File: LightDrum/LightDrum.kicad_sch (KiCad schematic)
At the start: 27 parts, among them U1 24LC04, Y1 16MHz

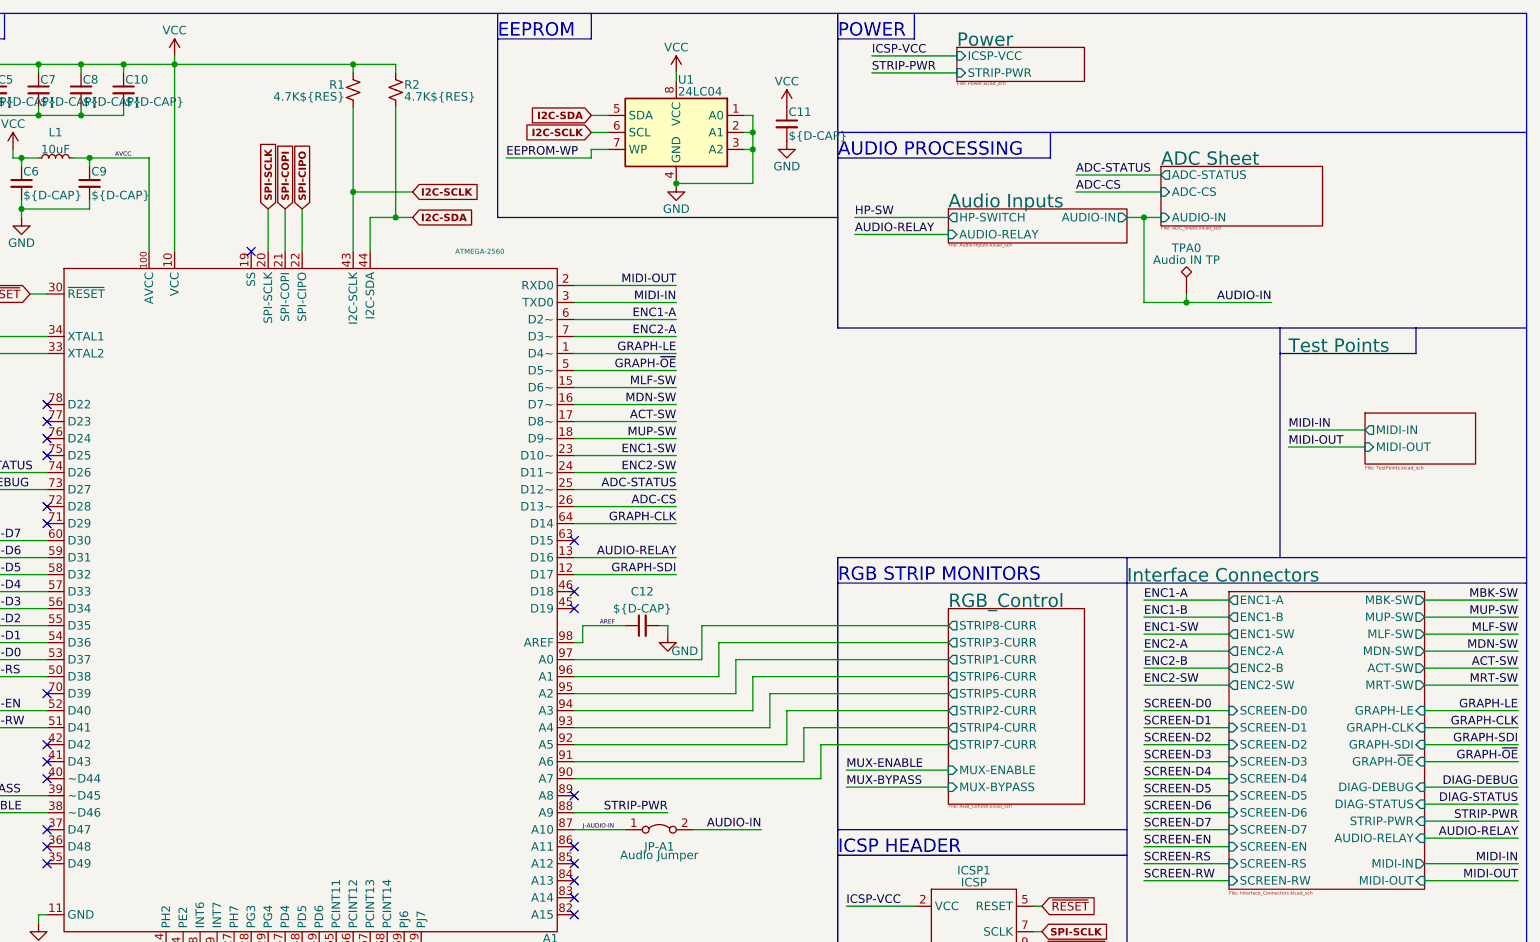
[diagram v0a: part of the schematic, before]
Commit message: Replace interface harnesses with FPC cable
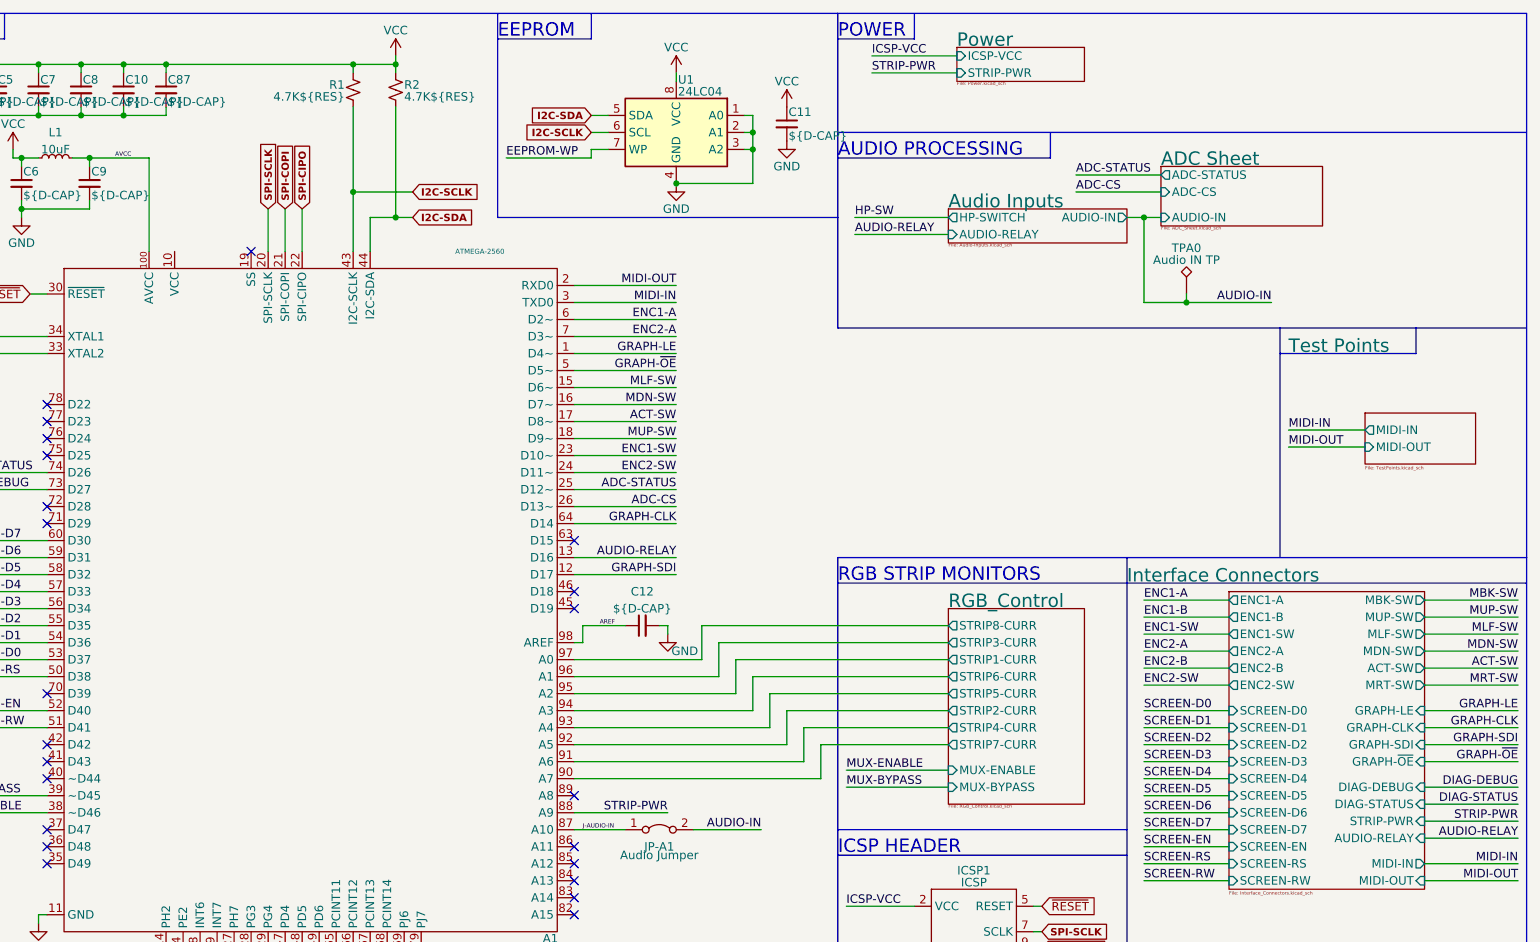
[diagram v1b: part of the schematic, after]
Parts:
- added C87: ${D-CAP}, Capacitor_SMD:C_0603_1608Metric, symbol Device:C_Small
- TPA0: footprint TestPoint:TestPoint_Loop_D2.50mm_Drill1.0mm_LowProfile -> TestPoint:TestPoint_Loop_D2.54mm_Drill1.5mm_Beaded
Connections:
- net GND: now also C87.2
- net VCC: now also C87.1

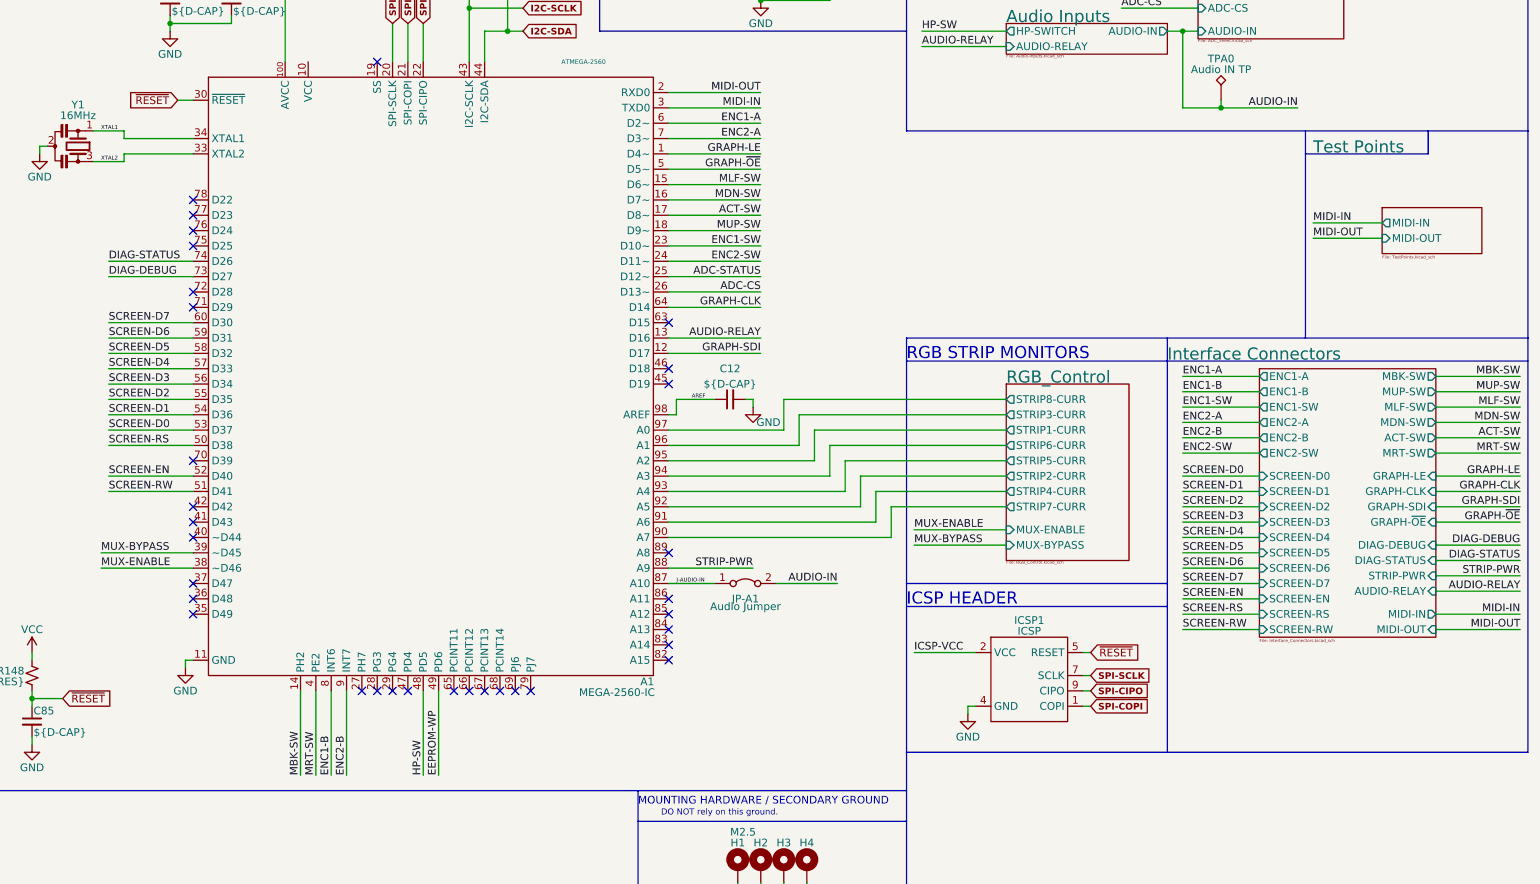
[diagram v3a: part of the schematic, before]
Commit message: Replace screen (WIP)
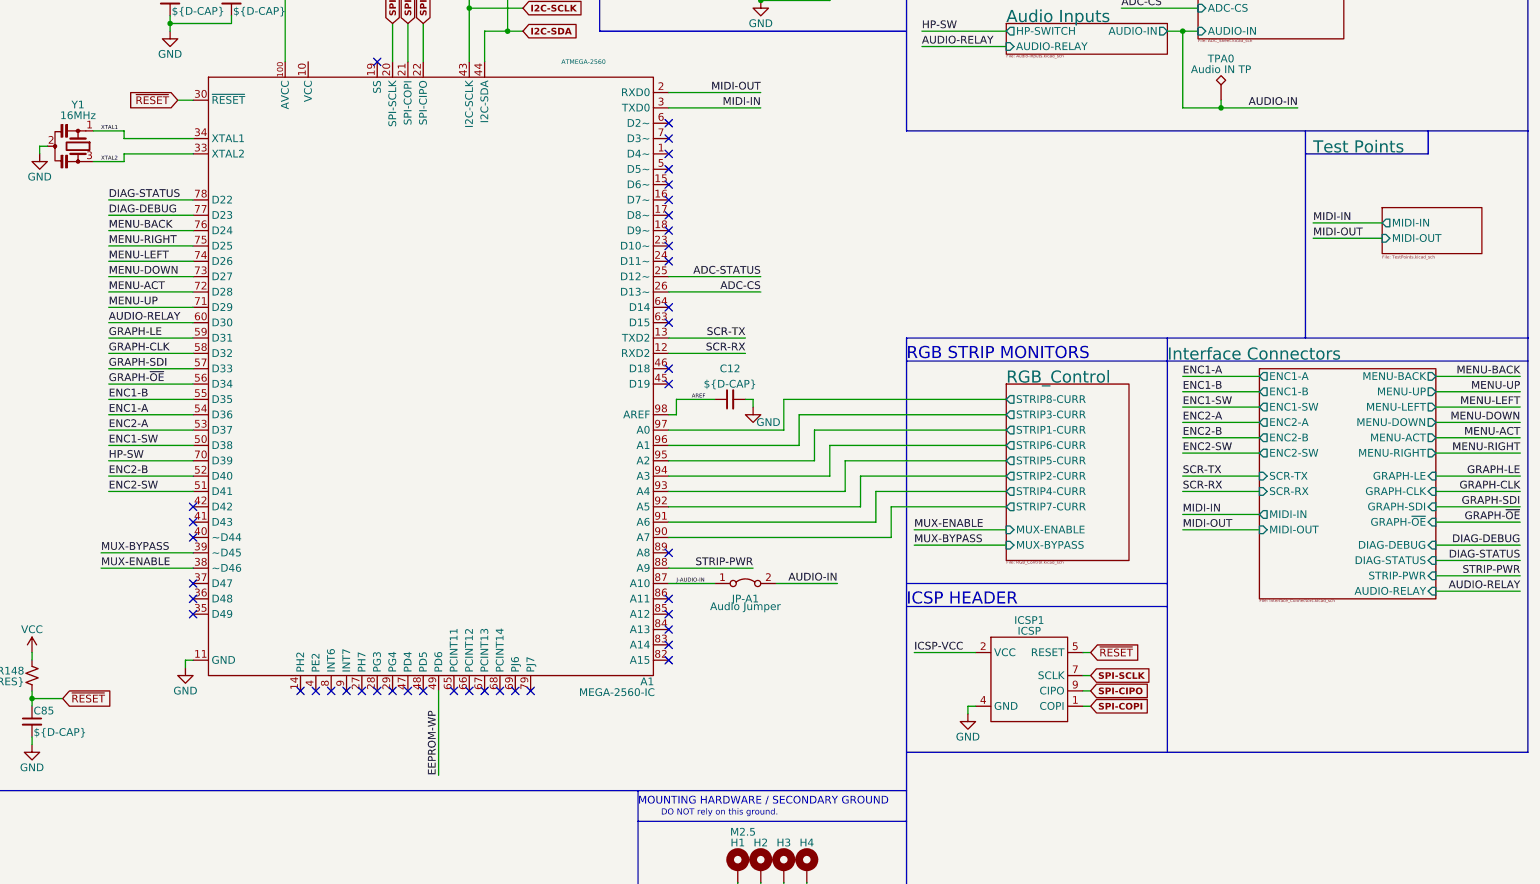
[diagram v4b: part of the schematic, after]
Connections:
- net SCREEN-D0 is gone; now on net ENC2-A: A1.53 (D37)
- net SCREEN-D1 is gone; now on net ENC1-A: A1.54 (D36)
- net SCREEN-D2 is gone; now on net ENC1-B: A1.55 (D35)
- net SCREEN-D3 is gone; now on net GRAPH-~{OE}: A1.56 (D34)
- net SCREEN-D4 is gone; now on net GRAPH-SDI: A1.57 (D33)
- net SCREEN-D5 is gone; now on net GRAPH-CLK: A1.58 (D32)
- net SCREEN-D6 is gone; now on net GRAPH-LE: A1.59 (D31)
- net SCREEN-D7 is gone; now on net AUDIO-RELAY: A1.60 (D30)
- net SCREEN-EN is gone; now on net ENC2-B: A1.52 (D40)
- net SCREEN-RS is gone; now on net ENC1-SW: A1.50 (D38)
- net SCREEN-RW is gone; now on net ENC2-SW: A1.51 (D41)
- net AUDIO-RELAY: no longer A1.13 (D16)
- net DIAG-DEBUG: now also A1.77 (D23); no longer A1.73 (D27)
- net DIAG-STATUS: now also A1.78 (D22); no longer A1.74 (D26)
- net ENC1-A: no longer A1.6 (D2~)
- net ENC1-B: no longer A1.8 (PE6)
- net ENC1-SW: no longer A1.23 (D10~)
- net ENC2-A: no longer A1.7 (D3~)
- net ENC2-B: no longer A1.9 (PE7)
- net ENC2-SW: no longer A1.24 (D11~)
- net GRAPH-CLK: no longer A1.64 (D14)
- net GRAPH-LE: no longer A1.1 (D4~)
- net GRAPH-SDI: no longer A1.12 (D17)
- net GRAPH-~{OE}: no longer A1.5 (D5~)
- net HP-SW: now also A1.70 (D39); no longer A1.48 (PD5)
- net MENU-UP: now reaches A1.71 (D29)
- net MENU-ACT: now reaches A1.72 (D28)
- net MENU-RIGHT: now reaches A1.75 (D25)
- net MENU-BACK: now reaches A1.76 (D24)
- net ACT-SW: no longer names the net of A1.17 (D8~)
- net MBK-SW: no longer names the net of A1.14 (PH2)
- net MDN-SW: no longer names the net of A1.16 (D7~)
- net MLF-SW: no longer names the net of A1.15 (D6~)
- net MRT-SW: no longer names the net of A1.4 (PE2)
- net MUP-SW: no longer names the net of A1.18 (D9~)
- new net MENU-DOWN: A1.73 (D27)
- new net MENU-LEFT: A1.74 (D26)
- new net SCR-RX: A1.12 (D17)
- new net SCR-TX: A1.13 (D16)
- no-connect marks 33 -> 42
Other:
- sheet Interface Connectors ports: added MENU-ACT, MENU-BACK, MENU-DOWN, MENU-LEFT, MENU-RIGHT, MENU-UP, SCR-RX, SCR-TX; removed ACT-SW, MBK-SW, MDN-SW, MLF-SW, MRT-SW, MUP-SW, SCREEN-D0, SCREEN-D1, SCREEN-D2, SCREEN-D3, SCREEN-D4, SCREEN-D5, SCREEN-D6, SCREEN-D7, SCREEN-EN, SCREEN-RS, SCREEN-RW

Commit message: Replaced display and FPC cable
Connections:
- net DIAG-DEBUG: now also A1.78 (D22); no longer A1.77 (D23)
- net DIAG-STATUS: now also A1.77 (D23); no longer A1.78 (D22)
- net MENU-BACK: now also A1.75 (D25); no longer A1.76 (D24)
- net MENU-RIGHT: now also A1.76 (D24); no longer A1.75 (D25)
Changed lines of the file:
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@@
     (effects (font (size 1.27 1.27)) (justify right bottom))
   )
-  (label "MENU-RIGHT" (at 39.37 82.55 0)
+  (label "MENU-RIGHT" (at 39.37 80.01 0)
     (effects (font (size 1.27 1.27)) (justify left bottom))
   )
@@
     (effects (font (size 1.27 1.27)) (justify right bottom))
   )
-  (label "MENU-BACK" (at 39.37 80.01 0)
+  (label "MENU-BACK" (at 39.37 82.55 0)
     (effects (font (size 1.27 1.27)) (justify left bottom))
   )
@@
     (effects (font (size 1.27 1.27)) (justify left bottom))
   )
-  (label "DIAG-STATUS" (at 39.37 74.93 0)
+  (label "DIAG-STATUS" (at 39.37 77.47 0)
     (effects (font (size 1.27 1.27)) (justify left bottom))
   )
@@
     (effects (font (size 1.27 1.27)) (justify right bottom))
   )
-  (label "DIAG-DEBUG" (at 39.37 77.47 0)
+  (label "DIAG-DEBUG" (at 39.37 74.93 0)
     (effects (font (size 1.27 1.27)) (justify left bottom))
   )

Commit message: First pass over schematic (WIP)
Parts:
- removed A1: MEGA-2560-IC, Package_QFP:TQFP-100_14x14mm_P0.5mm, symbol Daxxn_Arduino:MEGA-2560-IC
- removed C12: ${D-CAP}, Capacitor_SMD:C_0603_1608Metric, symbol Device:C_Small
- removed ICSP1: ICSP, Connector:Tag-Connect_TC2050-IDC-FP_2x05_P1.27mm_Vertical, symbol Daxxn_Connectors:ICSP
- removed L1: 10uF, Inductor_SMD:L_1210_3225Metric, symbol Device:L_Small
- removed TPA0: Audio IN TP, TestPoint:TestPoint_Loop_D2.54mm_Drill1.5mm_Beaded, symbol Connector:TestPoint_Alt
- added FB1: 120, Inductor_SMD:L_0603_1608Metric, symbol Device:FerriteBead_Small
- added J10: JTAG, Connector:Tag-Connect_TC2050-IDC-FP_2x05_P1.27mm_Vertical, symbol Connector:Conn_ARM_JTAG_SWD_10
- added J9: VBAT-CONN, symbol Connector:Conn_01x02_Male
- added Q1: RQ5A030AP, Package_TO_SOT_SMD:SOT-23, symbol Daxxn_Transistors:RQ5A030AP
- added R3: 10K, Resistor_SMD:R_0603_1608Metric, symbol Device:R_Small_US
- added SW1: SW_SPDT, Daxxn_Switches:EG1218, symbol Switch:SW_SPDT
- added U2: STM32F103VEH6, Daxxn_Packages:LFBGA-100_P0.8mm, symbol Daxxn_MicroControllers:STM32F103VEH6
- C1, C10, C11, C2, C3, C4, C5, C7, C8, C85, C87: value ${D-CAP} -> 100nF
- C6: value ${D-CAP} -> 10nF; footprint Capacitor_SMD:C_0805_2012Metric -> Capacitor_SMD:C_0603_1608Metric
- C9: value ${D-CAP} -> 100nF; footprint Capacitor_SMD:C_0805_2012Metric -> Capacitor_SMD:C_0603_1608Metric
- R1, R2: value 4.7K${RES} -> 2.2K; footprint Resistor_SMD:R_0805_2012Metric -> Resistor_SMD:R_0603_1608Metric
- R148: value ${P-RES} -> 10K; footprint Resistor_SMD:R_0805_2012Metric -> Resistor_SMD:R_0603_1608Metric
- Y1: value 16MHz -> 8MHz
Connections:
- net ADC-CS: now also U2.K7 (PB12)
- net AUDIO-RELAY: now also U2.B5 (PD5), U2.D7 (PD0)
- net DIAG-DEBUG: now also U2.B6 (PD2)
- net DIAG-STATUS: now also U2.C6 (PD3)
- net EEPROM-WP: now also U2.A3 (PB9)
- net ENC1-A: now also U2.H4 (PE7)
- net ENC1-B: now also U2.E2 (PE6)
- net ENC1-SW: now also U2.K4 (PE9)
- net ENC2-A: now also U2.J4 (PE8)
- net ENC2-B: now also U2.H5 (PE11)
- net ENC2-SW: now also U2.J5 (PE12)
- net GND: now also J10.3 (GND), J10.5 (GND), J10.9 (GNDDetect), Q1.1 (G), SW1.3 (C), U2.C1 (VSS_5), U2.E3 (VSS_4), U2.E4 (VSS_3), U2.E5 (VSS_2), U2.E6 (VSS_1), U2.G0 (VSSA), U2.H0 (VREF-)
- net GRAPH-CLK: now also U2.H2 (PA5)
- net GRAPH-LE: now also U2.D8 (PA8)
- net GRAPH-SDI: now also U2.K2 (PA7)
- net GRAPH-~{OE}: now also U2.C8 (PA9)
- net HP-SW: now also U2.D5 (PD7), U2.G5 (PE10)
- net I2C-SCLK: now also U2.B4 (PB6)
- net I2C-SDA: now also U2.A4 (PB7)
- net J-AUDIO-IN: now also U2.G2 (PA4)
- net MENU-ACT: now also U2.C2 (PE4)
- net MENU-BACK: now also U2.C3 (PE1)
- net MENU-DOWN: now also U2.B2 (PE3)
- net MENU-LEFT: now also U2.A2 (PE2)
- net MENU-RIGHT: now also U2.D3 (PE0)
- net MENU-UP: now also U2.D2 (PE5)
- net MIDI-IN: now also U2.K1 (PA3)
- net MIDI-OUT: now also U2.J1 (PA2)
- net SCR-RX: now also U2.K6 (PB11)
- net SCR-TX: now also U2.J6 (PB10)
- net SPI-CIPO: now also U2.H7 (PB14)
- net SPI-COPI: now also U2.G7 (PB15)
- net SPI-SCLK: now also U2.J7 (PB13)
- net STRIP-PWR: now also U2.D6 (PD4)
- net VCC: no longer C1.1, C10.1, C2.1, C3.1, C4.1, C5.1, C6.1, C7.1, C8.1, C87.1, R1.1, R2.1
- net XTAL1: now also U2.C0 (OSC_IN)
- net XTAL2: now also U2.D0 (OSC_OUT)
- net ~{RESET}: now also J10.10 (~{RESET}), U2.E0 (~{RST})
- net AVCC: no longer names the net of C9.1
- net AVCC: now also FB1.1, U2.K0 (VDDA)
- new net: R3.1, SW1.2 (B)
- new net: J10.1 (VTref), Q1.2 (S)
- new net: R3.2, U2.D4 (BOOT0)
- new net PWM-OE: U2.K8 (PD8)
- new net STRIP1-CURR: U2.G1 (PA0)
- new net STRIP2-CURR: U2.H1 (PA1)
- new net STRIP3-CURR: U2.F0 (PC0)
- new net STRIP4-CURR: U2.F1 (PC1)
- new net STRIP5-CURR: U2.E1 (PC2)
- new net STRIP6-CURR: U2.F2 (PC3)
- new net STRIP7-CURR: U2.G3 (PC4)
- new net STRIP8-CURR: U2.H3 (PC5)
- new net SWDCLK: J10.4 (SWDCLK/TCK), U2.A8 (JTMS-SWCLK)
- new net SWDIO: J10.2 (SWDIO/TMS), U2.A9 (JTMS-SWDIO)
- new net SWO: J10.6 (SWO/TDO), U2.A6 (JTDO)
- new net VBAT: J9.2 (Pin_2), U2.B1 (VBAT)
- new net VDD: C1.1, C10.1, C2.1, C3.1, C4.1, C5.1, C6.1, C7.1, C8.1, C87.1, FB1.2, J9.1 (Pin_1), Q1.3 (D), R1.1, R2.1, SW1.1 (A), U2.D1 (VDD_5), U2.F3 (VDD_4), U2.F4 (VDD_3), U2.F5 (VDD_2), U2.F6 (VDD_1), U2.J0 (VREF+)
- no-connect marks 42 -> 34
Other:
- removed sheet ADC Sheet
- sheet Audio Inputs ports: added HP-ADC-CS, HP-SEL-IND, HP-VREF-PG, XLR-ADC-CS, XLR-SEL-IND, XLR-VREF, XLR-VREF-PG; removed AUDIO-IN
- sheet RGB_Control ports: added ~{PWM-OE}; removed MUX-BYPASS, MUX-ENABLE
- note removed: "AUDIO PROCESSING"
- note removed: "EEPROM"
- note removed: "ICSP HEADER"
- note removed: "MICROCONTROLLER"
- note removed: "POWER"
- note removed: "RGB STRIP MONITORS"
- moved on the sheet: C1, C10, C11, C2, C3, C4, C5, C7, C8, C85, C87, H1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

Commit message: Clean up and remove old files
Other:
- sheet Audio Inputs ports: added none; removed XLR-VREF
- moved on the sheet: C1, C10, C11, C2, C3, C4, C5, C6, C7, C8, C85, C87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

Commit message: General component placement
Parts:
- removed J9: VBAT-CONN, symbol Connector:Conn_01x02_Male
- removed JP-A1: Audio Jumper, Jumper:SolderJumper-2_P1.3mm_Open_TrianglePad1.0x1.5mm, symbol Jumper:Jumper_2_Bridged
- added C114, C115: 10pF, Capacitor_SMD:C_0402_1005Metric, symbol Device:C_Small
- added Y102: 32.768KHz, Crystal:Crystal_SMD_MicroCrystal_CC7V-T1A-2Pin_3.2x1.5mm, symbol Device:Crystal_Small
- C101: renamed from C85; footprint Capacitor_SMD:C_0603_1608Metric -> Capacitor_SMD:C_0402_1005Metric
- C102: renamed from C11; footprint Capacitor_SMD:C_0603_1608Metric -> Capacitor_SMD:C_0402_1005Metric
- C103: renamed from C6; footprint Capacitor_SMD:C_0603_1608Metric -> Capacitor_SMD:C_0402_1005Metric
- C104: renamed from C1; footprint Capacitor_SMD:C_0603_1608Metric -> Capacitor_SMD:C_0402_1005Metric
- C105: renamed from C2; footprint Capacitor_SMD:C_0603_1608Metric -> Capacitor_SMD:C_0402_1005Metric
- C106: renamed from C3; footprint Capacitor_SMD:C_0603_1608Metric -> Capacitor_SMD:C_0402_1005Metric
- C107: renamed from C4; footprint Capacitor_SMD:C_0603_1608Metric -> Capacitor_SMD:C_0402_1005Metric
- C108: renamed from C5; footprint Capacitor_SMD:C_0603_1608Metric -> Capacitor_SMD:C_0402_1005Metric
- C109: renamed from C7; footprint Capacitor_SMD:C_0603_1608Metric -> Capacitor_SMD:C_0402_1005Metric
- C110: renamed from C8; footprint Capacitor_SMD:C_0603_1608Metric -> Capacitor_SMD:C_0402_1005Metric
- C111: renamed from C10; footprint Capacitor_SMD:C_0603_1608Metric -> Capacitor_SMD:C_0402_1005Metric
- C112: renamed from C87; footprint Capacitor_SMD:C_0603_1608Metric -> Capacitor_SMD:C_0402_1005Metric
- C113: renamed from C9; footprint Capacitor_SMD:C_0603_1608Metric -> Capacitor_SMD:C_0402_1005Metric
- R101: renamed from R148; footprint Resistor_SMD:R_0603_1608Metric -> Resistor_SMD:R_0402_1005Metric
- R102: renamed from R3; footprint Resistor_SMD:R_0603_1608Metric -> Resistor_SMD:R_0402_1005Metric
- R103: renamed from R1; footprint Resistor_SMD:R_0603_1608Metric -> Resistor_SMD:R_0402_1005Metric
- R104: renamed from R2; footprint Resistor_SMD:R_0603_1608Metric -> Resistor_SMD:R_0402_1005Metric
- renumbered FB1 to FB101, J10 to J102, Q1 to Q101, SW1 to SW101, U2 to U101, U1 to U102, Y1 to Y101
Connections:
- net GND: now also C114.2, C115.2
- net SCR-RX: now also U101.J6 (PB10); no longer U101.K6 (PB11)
- net SCR-TX: now also U101.K6 (PB11); no longer U101.J6 (PB10)
- net at U101.A0 (PC14): now also C114.1, Y102.1
- net RTC-OUT: now reaches U101.A1 (PC13)
- net at U101.B0 (PC15): now also C115.1, Y102.2
- net CHG-STATUS: now reaches U101.C7 (PC12)
- net J-AUDIO-IN: no longer names the net of U101.G2 (PA4)
- no-connect marks 34 -> 31
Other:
- added sheet Battery Charger (Battery-Charger.kicad_sch)
- moved on the sheet: C101, C103, C113, R101
